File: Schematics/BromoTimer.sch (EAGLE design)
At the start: 19 parts, among them IC1 PIC16F687, IC2 7805TV, K1 351, K2 351, Q1 2N3565, Q2 2N3565

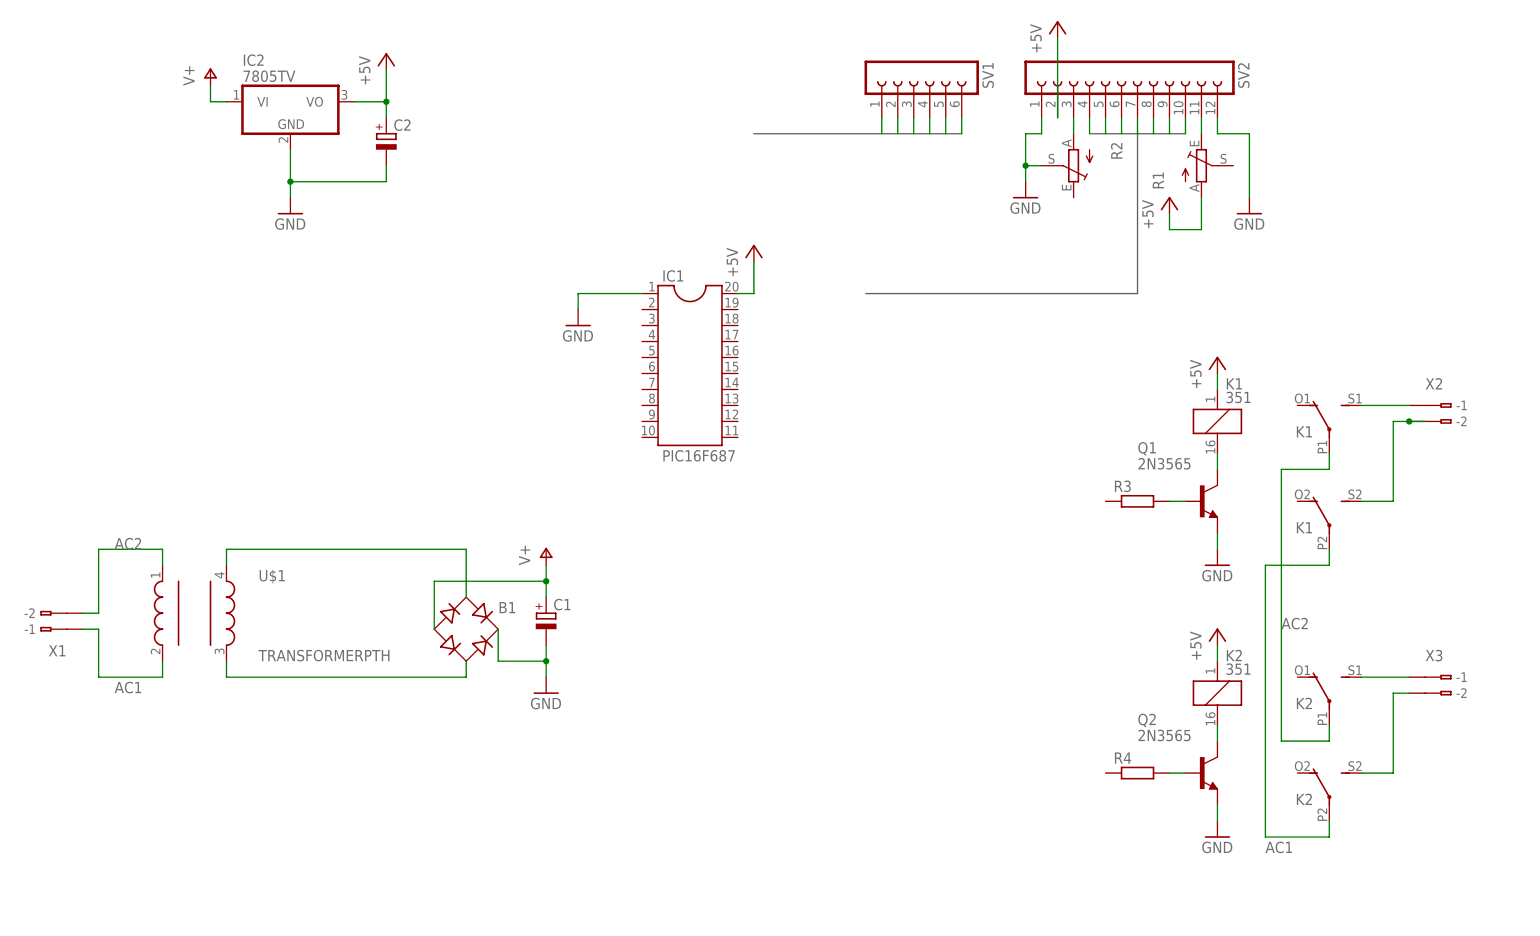
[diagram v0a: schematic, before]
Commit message: Finished first version of the schematic.
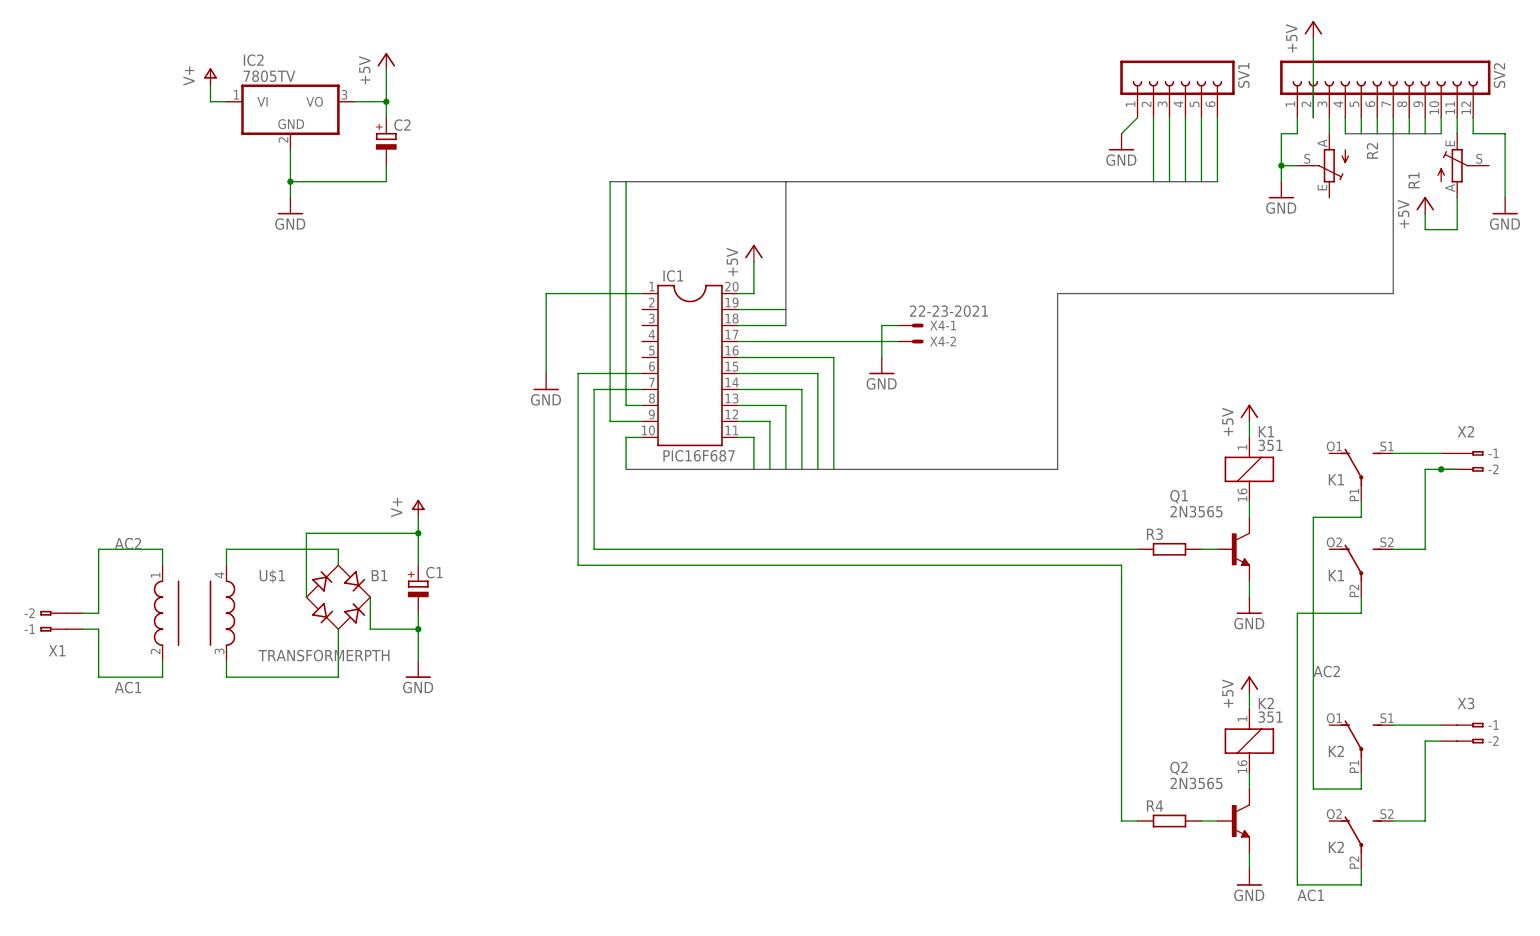
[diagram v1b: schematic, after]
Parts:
- added X4: 22-23-2021, con-molex:22-23-2021
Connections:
- new net N$13: IC1.17, X4-2.S
- new net N$14: IC1.6, R4.1
- new net N$16: IC1.7, R3.1
- net A: now also IC1.19
- net B: now also IC1.18
- net B0: now also IC1.13
- net B1: now also IC1.12
- net B2: now also IC1.11
- net B3: now also IC1.10
- net EN: now also IC1.16
- net GND: now also X4-1.S
- net L1: now also IC1.8
- net L2: now also IC1.9
- net RS: now also IC1.15
- net RW: now also IC1.14
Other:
- moved on the sheet: B1, C1, K1, K2, Q1, Q2, R1, R2, R3, R4, SV1, SV2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

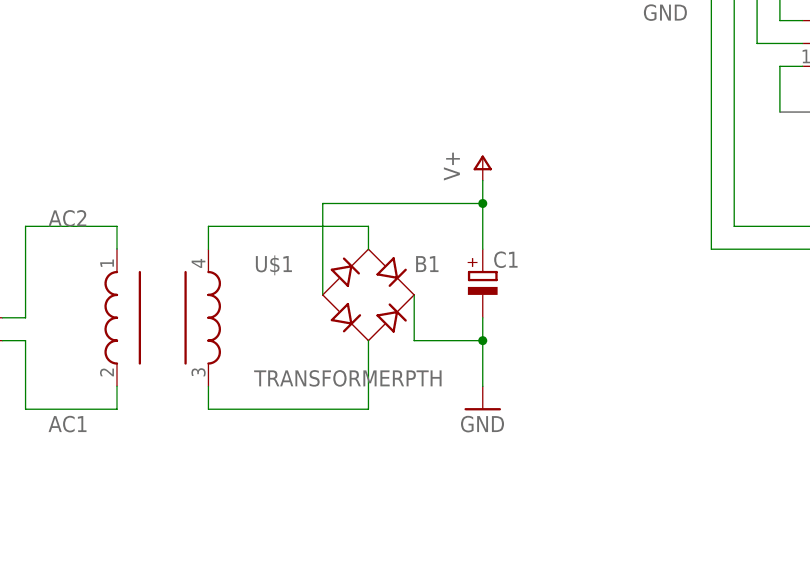
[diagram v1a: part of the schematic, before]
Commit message: Fixed bug in schematics
The poles on the diode bridge were inverted.
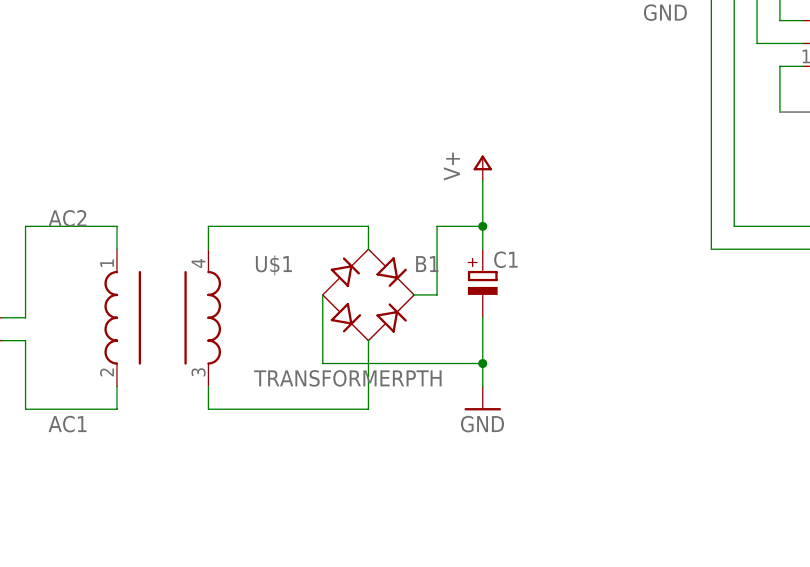
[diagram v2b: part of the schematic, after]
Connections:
- net GND: now also B1.-; no longer B1.+
- net V+: now also B1.+; no longer B1.-
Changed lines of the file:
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@@
 <?xml version="1.0" encoding="utf-8"?>
 <!DOCTYPE eagle SYSTEM "eagle.dtd">
-<eagle version="6.2">
+<eagle version="6.3">
 <drawing>
 <settings>
@@
 <segment>
 <pinref part="C1" gate="G$1" pin="-"/>
-<wire x1="73.66" y1="76.2" x2="73.66" y2="73.66" width="0.1524" layer="91"/>
-<pinref part="B1" gate="1" pin="+"/>
-<wire x1="73.66" y1="73.66" x2="66.04" y2="73.66" width="0.1524" layer="91"/>
-<wire x1="66.04" y1="73.66" x2="66.04" y2="78.74" width="0.1524" layer="91"/>
 <pinref part="GND7" gate="1" pin="GND"/>
-<wire x1="73.66" y1="68.58" x2="73.66" y2="73.66" width="0.1524" layer="91"/>
-<junction x="73.66" y="73.66"/>
+<wire x1="73.66" y1="68.58" x2="73.66" y2="71.12" width="0.1524" layer="91"/>
+<pinref part="B1" gate="1" pin="-"/>
+<wire x1="73.66" y1="71.12" x2="73.66" y2="76.2" width="0.1524" layer="91"/>
+<wire x1="55.88" y1="78.74" x2="55.88" y2="71.12" width="0.1524" layer="91"/>
+<wire x1="55.88" y1="71.12" x2="73.66" y2="71.12" width="0.1524" layer="91"/>
+<junction x="73.66" y="71.12"/>
 </segment>
 <segment>
@@
 <net name="V+" class="0">
 <segment>
-<pinref part="B1" gate="1" pin="-"/>
-<wire x1="55.88" y1="78.74" x2="55.88" y2="88.9" width="0.1524" layer="91"/>
 <pinref part="C1" gate="G$1" pin="+"/>
-<wire x1="55.88" y1="88.9" x2="73.66" y2="88.9" width="0.1524" layer="91"/>
-<wire x1="73.66" y1="88.9" x2="73.66" y2="83.82" width="0.1524" layer="91"/>
+<wire x1="73.66" y1="91.44" x2="73.66" y2="86.36" width="0.1524" layer="91"/>
 <pinref part="P+7" gate="1" pin="V+"/>
-<wire x1="73.66" y1="91.44" x2="73.66" y2="88.9" width="0.1524" layer="91"/>
-<junction x="73.66" y="88.9"/>
-</segment>
-<segment>
+<pinref part="B1" gate="1" pin="+"/>
+<wire x1="73.66" y1="86.36" x2="73.66" y2="83.82" width="0.1524" layer="91"/>
+<wire x1="66.04" y1="78.74" x2="68.58" y2="78.74" width="0.1524" layer="91"/>
+<wire x1="68.58" y1="78.74" x2="68.58" y2="86.36" width="0.1524" layer="91"/>
+<wire x1="68.58" y1="86.36" x2="73.66" y2="86.36" width="0.1524" layer="91"/>
+<junction x="73.66" y="86.36"/>
+</segment>
+<segment>

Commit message: Use 12V relay.
Use 12V relay since V relays are not common.
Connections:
- net +5V: no longer K11.1, K21.1
- net V+: now also K11.1, K21.1
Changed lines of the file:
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@@
 <part name="K1" library="relay" deviceset="351" device=""/>
 <part name="K2" library="relay" deviceset="351" device=""/>
-<part name="P+5" library="supply1" deviceset="+5V" device=""/>
-<part name="P+6" library="supply1" deviceset="+5V" device=""/>
 <part name="U$1" library="SparkFun" deviceset="TRANSFORMER" device="PTH"/>
 <part name="B1" library="rectifier" deviceset="RB1A" device=""/>
@@
 <part name="GND8" library="supply1" deviceset="GND" device=""/>
 <part name="GND9" library="supply1" deviceset="GND" device=""/>
+<part name="P+5" library="supply1" deviceset="V+" device=""/>
+<part name="P+6" library="supply1" deviceset="V+" device=""/>
 </parts>
 <sheets>
@@
 <instance part="K2" gate="2" x="223.52" y="53.34" rot="MR0"/>
 <instance part="K2" gate="3" x="223.52" y="38.1" rot="MR0"/>
-<instance part="P+5" gate="1" x="205.74" y="109.22"/>
-<instance part="P+6" gate="1" x="205.74" y="66.04"/>
 <instance part="U$1" gate="G$1" x="38.1" y="76.2"/>
 <instance part="B1" gate="1" x="60.96" y="78.74"/>
@@
 <instance part="GND8" gate="1" x="185.42" y="149.86"/>
 <instance part="GND9" gate="1" x="147.32" y="114.3"/>
+<instance part="P+5" gate="1" x="205.74" y="66.04"/>
+<instance part="P+6" gate="1" x="205.74" y="109.22"/>
 </instances>
 <busses>
@@
 <wire x1="233.68" y1="137.16" x2="238.76" y2="137.16" width="0.1524" layer="91"/>
 <wire x1="238.76" y1="137.16" x2="238.76" y2="142.24" width="0.1524" layer="91"/>
-</segment>
-<segment>
-<pinref part="P+5" gate="1" pin="+5V"/>
-<pinref part="K1" gate="1" pin="1"/>
-<wire x1="205.74" y1="106.68" x2="205.74" y2="104.14" width="0.1524" layer="91"/>
-</segment>
-<segment>
-<pinref part="P+6" gate="1" pin="+5V"/>
-<pinref part="K2" gate="1" pin="1"/>
-<wire x1="205.74" y1="63.5" x2="205.74" y2="60.96" width="0.1524" layer="91"/>
 </segment>
 </net>
@@
 <wire x1="40.64" y1="157.48" x2="43.18" y2="157.48" width="0.1524" layer="91"/>
 </segment>
-</net>
+<segment>
+<pinref part="K2" gate="1" pin="1"/>
+<wire x1="205.74" y1="63.5" x2="205.74" y2="60.96" width="0.1524" layer="91"/>
+<pinref part="P+5" gate="1" pin="V+"/>
+</segment>
+<segment>
+<pinref part="K1" gate="1" pin="1"/>
+<wire x1="205.74" y1="106.68" x2="205.74" y2="104.14" width="0.1524" layer="91"/>
+<pinref part="P+6" gate="1" pin="V+"/>
+</segment>
+</net>

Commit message: Add ICSP header
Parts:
- added D1, D2: 1N4148DO35-7, diode:1N4148DO35-7
- added SV3: (no value), con-lstb:MA05-1
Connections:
- new net N$15: IC1.4, SV3.1
- net +5V: now also SV3.2
- net A: now also SV3.4
- net B: now also SV3.5
- net GND: now also D1.A, D2.A, SV3.3
- net V+: now also D1.C, D2.C
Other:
- moved on the sheet: R3, R4
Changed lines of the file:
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@@
 <part name="P+5" library="supply1" deviceset="V+" device=""/>
 <part name="P+6" library="supply1" deviceset="V+" device=""/>
+<part name="D1" library="diode" deviceset="1N4148" device="DO35-7"/>
+<part name="D2" library="diode" deviceset="1N4148" device="DO35-7"/>
+<part name="SV3" library="con-lstb" deviceset="MA05-1" device=""/>
+<part name="P+9" library="supply1" deviceset="+5V" device=""/>
+<part name="GND10" library="supply1" deviceset="GND" device=""/>
 </parts>
 <sheets>
@@
 <instance part="Q1" gate="G$1" x="203.2" y="86.36"/>
 <instance part="Q2" gate="G$1" x="203.2" y="43.18"/>
-<instance part="R3" gate="G$1" x="193.04" y="86.36"/>
-<instance part="R4" gate="G$1" x="193.04" y="43.18"/>
-<instance part="GND5" gate="1" x="205.74" y="76.2"/>
-<instance part="GND6" gate="1" x="205.74" y="33.02"/>
+<instance part="R3" gate="G$1" x="180.34" y="86.36"/>
+<instance part="R4" gate="G$1" x="180.34" y="43.18"/>
+<instance part="GND5" gate="1" x="205.74" y="73.66"/>
+<instance part="GND6" gate="1" x="205.74" y="30.48"/>
 <instance part="X2" gate="G$1" x="243.84" y="101.6"/>
 <instance part="X3" gate="G$1" x="243.84" y="58.42"/>
@@
 <instance part="GND8" gate="1" x="185.42" y="149.86"/>
 <instance part="GND9" gate="1" x="147.32" y="114.3"/>
-<instance part="P+5" gate="1" x="205.74" y="66.04"/>
-<instance part="P+6" gate="1" x="205.74" y="109.22"/>
+<instance part="P+5" gate="1" x="205.74" y="68.58"/>
+<instance part="P+6" gate="1" x="205.74" y="111.76"/>
+<instance part="D1" gate="G$1" x="187.96" y="43.18" rot="R90"/>
+<instance part="D2" gate="G$1" x="187.96" y="86.36" rot="R90"/>
+<instance part="SV3" gate="G$1" x="134.62" y="170.18" rot="R270"/>
+<instance part="P+9" gate="1" x="119.38" y="165.1"/>
+<instance part="GND10" gate="1" x="134.62" y="154.94"/>
 </instances>
 <busses>
@@
 <wire x1="233.68" y1="137.16" x2="238.76" y2="137.16" width="0.1524" layer="91"/>
 <wire x1="238.76" y1="137.16" x2="238.76" y2="142.24" width="0.1524" layer="91"/>
+</segment>
+<segment>
+<pinref part="SV3" gate="G$1" pin="2"/>
+<wire x1="132.08" y1="162.56" x2="132.08" y2="157.48" width="0.1524" layer="91"/>
+<wire x1="132.08" y1="157.48" x2="119.38" y2="157.48" width="0.1524" layer="91"/>
+<wire x1="119.38" y1="157.48" x2="119.38" y2="162.56" width="0.1524" layer="91"/>
+<pinref part="P+9" gate="1" pin="+5V"/>
 </segment>
 </net>
@@
 <pinref part="GND5" gate="1" pin="GND"/>
 <wire x1="205.74" y1="81.28" x2="205.74" y2="78.74" width="0.1524" layer="91"/>
+<pinref part="D2" gate="G$1" pin="A"/>
+<wire x1="205.74" y1="78.74" x2="205.74" y2="76.2" width="0.1524" layer="91"/>
+<wire x1="187.96" y1="83.82" x2="187.96" y2="78.74" width="0.1524" layer="91"/>
+<wire x1="187.96" y1="78.74" x2="205.74" y2="78.74" width="0.1524" layer="91"/>
+<junction x="205.74" y="78.74"/>
 </segment>
 <segment>
@@
 <pinref part="GND6" gate="1" pin="GND"/>
 <wire x1="205.74" y1="38.1" x2="205.74" y2="35.56" width="0.1524" layer="91"/>
+<pinref part="D1" gate="G$1" pin="A"/>
+<wire x1="205.74" y1="35.56" x2="205.74" y2="33.02" width="0.1524" layer="91"/>
+<wire x1="187.96" y1="40.64" x2="187.96" y2="35.56" width="0.1524" layer="91"/>
+<wire x1="187.96" y1="35.56" x2="205.74" y2="35.56" width="0.1524" layer="91"/>
+<junction x="205.74" y="35.56"/>
 </segment>
 <segment>
@@
 <wire x1="147.32" y1="121.92" x2="147.32" y2="116.84" width="0.1524" layer="91"/>
 </segment>
+<segment>
+<pinref part="SV3" gate="G$1" pin="3"/>
+<pinref part="GND10" gate="1" pin="GND"/>
+<wire x1="134.62" y1="162.56" x2="134.62" y2="157.48" width="0.1524" layer="91"/>
+</segment>
 </net>
 <net name="RS" class="0">
@@
 <wire x1="124.46" y1="124.46" x2="132.08" y2="124.46" width="0.1524" layer="91"/>
 </segment>
+<segment>
+<pinref part="SV3" gate="G$1" pin="4"/>
+<wire x1="137.16" y1="162.56" x2="137.16" y2="144.78" width="0.1524" layer="91"/>
+</segment>
 </net>
 <net name="B" class="0">
@@
 <wire x1="124.46" y1="121.92" x2="132.08" y2="121.92" width="0.1524" layer="91"/>
 </segment>
+<segment>
+<pinref part="SV3" gate="G$1" pin="5"/>
+<wire x1="139.7" y1="162.56" x2="139.7" y2="144.78" width="0.1524" layer="91"/>
+</segment>
 </net>
 <net name="N$4" class="0">
@@
 <pinref part="R4" gate="G$1" pin="2"/>
 <pinref part="Q2" gate="G$1" pin="B"/>
-<wire x1="198.12" y1="43.18" x2="200.66" y2="43.18" width="0.1524" layer="91"/>
+<wire x1="185.42" y1="43.18" x2="200.66" y2="43.18" width="0.1524" layer="91"/>
 </segment>
 </net>
@@
 <pinref part="R3" gate="G$1" pin="2"/>
 <pinref part="Q1" gate="G$1" pin="B"/>
-<wire x1="198.12" y1="86.36" x2="200.66" y2="86.36" width="0.1524" layer="91"/>
+<wire x1="185.42" y1="86.36" x2="200.66" y2="86.36" width="0.1524" layer="91"/>
 </segment>
 </net>
@@
 <segment>
 <pinref part="K2" gate="1" pin="1"/>
+<wire x1="205.74" y1="66.04" x2="205.74" y2="63.5" width="0.1524" layer="91"/>
+<pinref part="P+5" gate="1" pin="V+"/>
+<pinref part="D1" gate="G$1" pin="C"/>
 <wire x1="205.74" y1="63.5" x2="205.74" y2="60.96" width="0.1524" layer="91"/>
-<pinref part="P+5" gate="1" pin="V+"/>
+<wire x1="187.96" y1="45.72" x2="187.96" y2="63.5" width="0.1524" layer="91"/>
+<wire x1="187.96" y1="63.5" x2="205.74" y2="63.5" width="0.1524" layer="91"/>
+<junction x="205.74" y="63.5"/>
 </segment>
 <segment>
 <pinref part="K1" gate="1" pin="1"/>
+<wire x1="205.74" y1="109.22" x2="205.74" y2="106.68" width="0.1524" layer="91"/>
+<pinref part="P+6" gate="1" pin="V+"/>
+<pinref part="D2" gate="G$1" pin="C"/>
 <wire x1="205.74" y1="106.68" x2="205.74" y2="104.14" width="0.1524" layer="91"/>
-<pinref part="P+6" gate="1" pin="V+"/>
+<wire x1="187.96" y1="88.9" x2="187.96" y2="106.68" width="0.1524" layer="91"/>
+<wire x1="187.96" y1="106.68" x2="205.74" y2="106.68" width="0.1524" layer="91"/>
+<junction x="205.74" y="106.68"/>
 </segment>
 </net>
@@
 <wire x1="109.22" y1="111.76" x2="101.6" y2="111.76" width="0.1524" layer="91"/>
 <wire x1="101.6" y1="111.76" x2="101.6" y2="86.36" width="0.1524" layer="91"/>
-<wire x1="101.6" y1="86.36" x2="187.96" y2="86.36" width="0.1524" layer="91"/>
+<wire x1="101.6" y1="86.36" x2="175.26" y2="86.36" width="0.1524" layer="91"/>
 </segment>
 </net>
@@
 <wire x1="109.22" y1="114.3" x2="99.06" y2="114.3" width="0.1524" layer="91"/>
 <wire x1="99.06" y1="114.3" x2="99.06" y2="83.82" width="0.1524" layer="91"/>
-<wire x1="99.06" y1="83.82" x2="185.42" y2="83.82" width="0.1524" layer="91"/>
+<wire x1="99.06" y1="83.82" x2="172.72" y2="83.82" width="0.1524" layer="91"/>
 <pinref part="R4" gate="G$1" pin="1"/>
-<wire x1="185.42" y1="83.82" x2="185.42" y2="43.18" width="0.1524" layer="91"/>
-<wire x1="185.42" y1="43.18" x2="187.96" y2="43.18" width="0.1524" layer="91"/>
-</segment>
-</net>
+<wire x1="172.72" y1="83.82" x2="172.72" y2="43.18" width="0.1524" layer="91"/>
+<wire x1="172.72" y1="43.18" x2="175.26" y2="43.18" width="0.1524" layer="91"/>
+</segment>
+</net>
+<net name="N$15" class="0">
+<segment>
+<pinref part="SV3" gate="G$1" pin="1"/>
+<wire x1="129.54" y1="162.56" x2="129.54" y2="160.02" width="0.1524" layer="91"/>
+<wire x1="129.54" y1="160.02" x2="99.06" y2="160.02" width="0.1524" layer="91"/>
+<pinref part="IC1" gate="G$1" pin="4"/>
+<wire x1="99.06" y1="160.02" x2="99.06" y2="119.38" width="0.1524" layer="91"/>
+<wire x1="99.06" y1="119.38" x2="109.22" y2="119.38" width="0.1524" layer="91"/>
+</segment>
+</net>
